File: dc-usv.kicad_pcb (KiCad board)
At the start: 4 copper layers, 160 x 100 mm, 297 parts, among them J1 Output 2.0mm, J2 Output 2.0mm, J3 Output 2.0mm, J5 HanRun_HR911105A, J6 USB_C_Receptacle_USB2.0, J7 Input 2.0mm, J8 Input 2.5mm, J9 USB_C_Receptacle_USB2.0, Q1 AON7544, Q10 AO4407A, Q11 2N7002, Q12 MMBT3904, Q13 2N7002, Q14 2N7002, Q15 2N7002, Q16 2N7002, Q17 2N7002, Q18 MMBT3904, Q19 AO4407A, Q2 AO3401A, Q20 2N7002, Q21 AO4407A, Q22 2N7002, Q23 AO4407A, Q24 2N7002, Q25 AO3401A, Q26 AO3401A, Q27 2N7002, Q28 MMBT3904, Q29 MMBT3904, Q3 AON7544, Q30 MMBT3904, Q31 2N7002, Q32 AO4407A, Q33 MMBT3904, Q34 2N7002, Q35 AO4407A, Q36 MMBT3904, Q37 2N7002, Q38 AO4407A, Q4 AON7544, Q5 AON7544, Q6 CSD17308Q3, Q7 CSD17308Q3, Q8 AO4407A, Q9 2N7002, SW1 SW_DIP_x02, U1 BQ40z50-R2, U10 LAN8720A, U11 74HC595, U12 SY8105, U13 LM75B, U14 INA219AxD, U15 INA219AxD, U16 CH340G, U2 LM75B, U3 BQ24715, U4 TPS61178x, U5 INA219AxD, U6 INA219AxD, U7 LM75B, U8 SY8120B1ABC, U9 ESP32-WROOM-32E, Y1 12MHz

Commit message: Charger and step-down component placement
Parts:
- removed Q26: AO3401A, Package_TO_SOT_SMD:SOT-23
- removed Q27: 2N7002, Package_TO_SOT_SMD:SOT-23
- removed R95: 100kR, Resistor_SMD:R_0402_1005Metric
- added D15: B5819W, Diode_SMD:D_SOD-123, F.Cu at (58.6, 70.1)
- added D16: P6SMB6.8CA, Diode_SMD:D_SMB, F.Cu at (168.1, 109.8)
- C77, C79: value 100nF HV -> 100nF; footprint Capacitor_SMD:C_0603_1608Metric -> Capacitor_SMD:C_0402_1005Metric
- moved R56 231.2 mm to (7.11, 46.9)
- moved R102 230.9 mm to (37.5, 26.9)
- moved Q29 229.7 mm to (38.3, 30.8), turned to -90 degrees
- moved R58 227.6 mm to (7.20, 50.7)
- moved Q28 223.3 mm to (41.8, 30.8), turned to -90 degrees
- moved R60 217.9 mm to (7.25, 53.7)
- moved R101 216.2 mm to (37.5, 28.2)
- moved C16 198.4 mm to (79.7, 84.3), turned to -90 degrees
- moved R17 198.1 mm to (81.8, 101.4)
- moved R61 197.6 mm to (40.8, 79.5), turned to 90 degrees
- moved R22 196.4 mm to (74.0, 99.9), turned to 180 degrees
- moved C12 194.5 mm to (79.4, 95.7)
- moved R53 194.3 mm to (37.8, 33.4)
- moved R93 193.2 mm to (55.8, 69.9), turned to 90 degrees
- moved R92 193.1 mm to (57.1, 66.0), turned to -90 degrees
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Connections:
- C77 pad 1: Net-(C77-Pad1) -> GND
- C77 pad 2: GND -> Net-(C78-Pad1)
- C78 pad 1: Net-(C77-Pad1) -> Net-(C78-Pad1)
- C79 pad 1: GND -> Net-(C78-Pad2)
- C79 pad 2: Net-(C78-Pad2) -> GND
- R80 pad 1: Net-(C77-Pad1) -> Net-(C78-Pad1)
- U14 pad 8: Net-(C77-Pad1) -> Net-(C78-Pad1)
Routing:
- net GND: track 3.25 -> 17.3 mm, vias 3 -> 8
- net +3V3: track 0.00 -> 13.2 mm, vias 0 -> 3
- net Net-(C52-Pad1): track 0.00 -> 9.57 mm
- net Net-(C54-Pad2): track 0.00 -> 5.42 mm
- net Net-(C54-Pad1): track 0.00 -> 4.58 mm
- net Net-(C58-Pad2): track 0.00 -> 3.65 mm
- net Net-(R51-Pad1): track 0.00 -> 1.01 mm

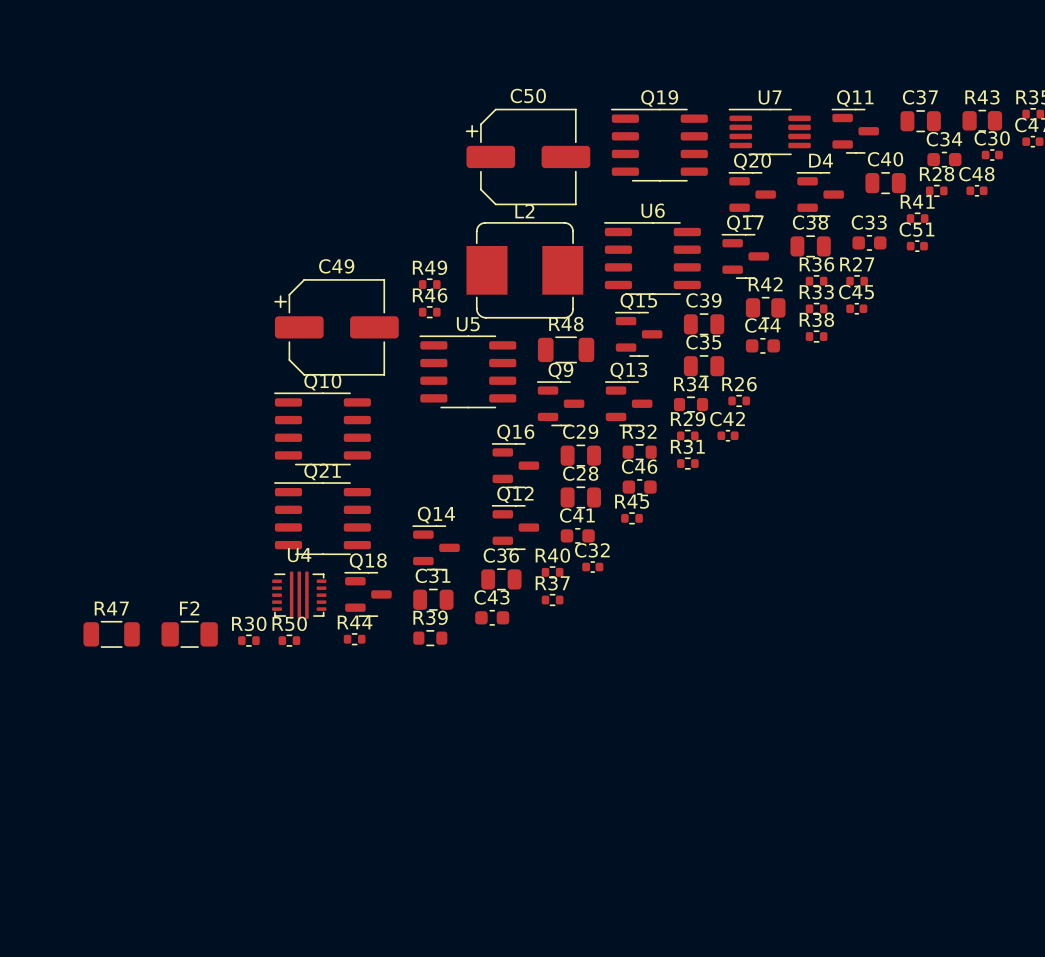
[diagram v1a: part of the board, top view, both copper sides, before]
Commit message: Partial DC out step-up component placement
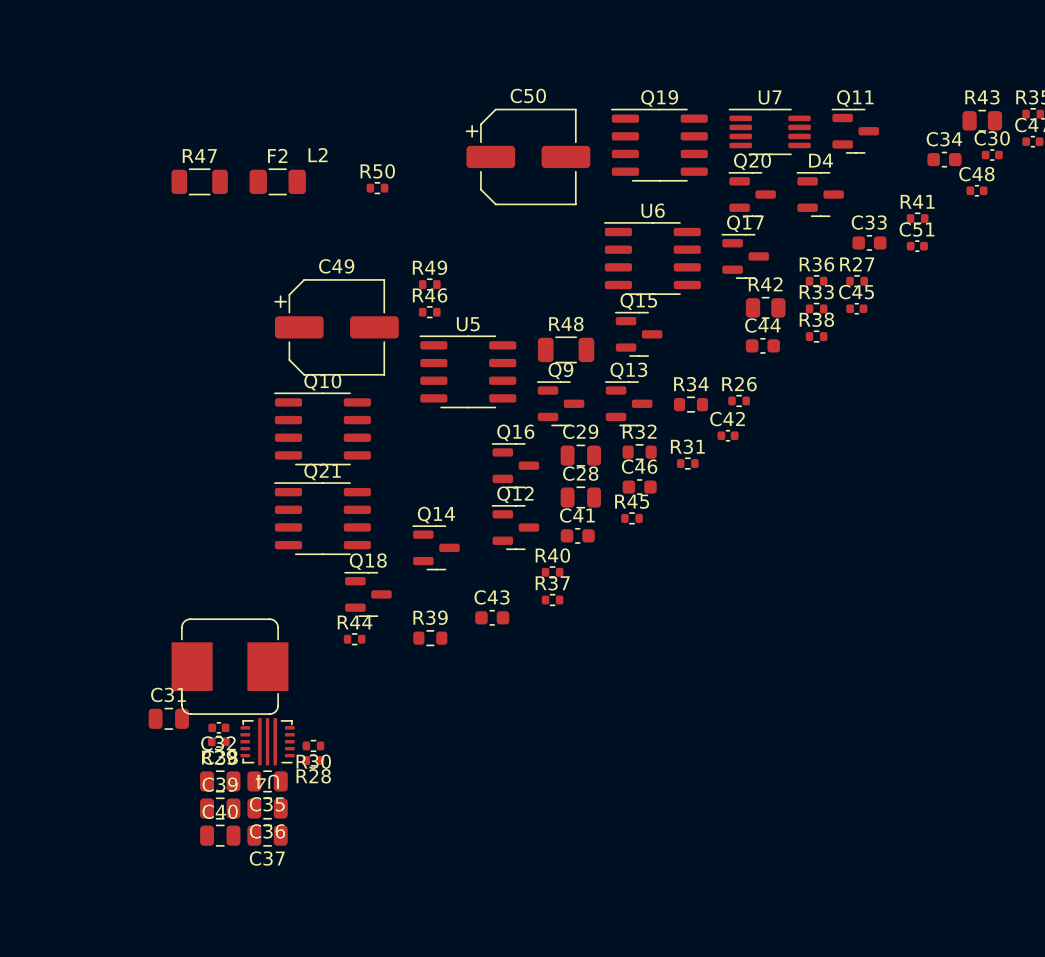
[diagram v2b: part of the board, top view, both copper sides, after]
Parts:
- moved C37 69.6 mm to (205.6, 71.4), turned to 180 degrees
- moved C40 67.0 mm to (202.2, 71.4)
- moved R28 60.7 mm to (208.8, 66.0), turned to 180 degrees
- moved C38 57.3 mm to (202.2, 67.5)
- moved C39 49.2 mm to (202.2, 69.5)
- moved C35 43.3 mm to (205.6, 67.5), turned to 180 degrees
- moved R29 40.2 mm to (202.1, 64.7), turned to 180 degrees
- moved L2 35.5 mm to (202.8, 59.2)
- moved F2 33.1 mm to (206.3, 24.4)
- moved R47 33.1 mm to (200.7, 24.4)
- moved R50 33.1 mm to (213.4, 24.9)
- moved C32 29.3 mm to (202.1, 63.6), turned to 180 degrees
- moved C36 23.5 mm to (205.6, 69.5), turned to 180 degrees
- moved C31 20.9 mm to (198.4, 63.0)
- moved U4 10.8 mm to (205.6, 64.7), turned to 180 degrees
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
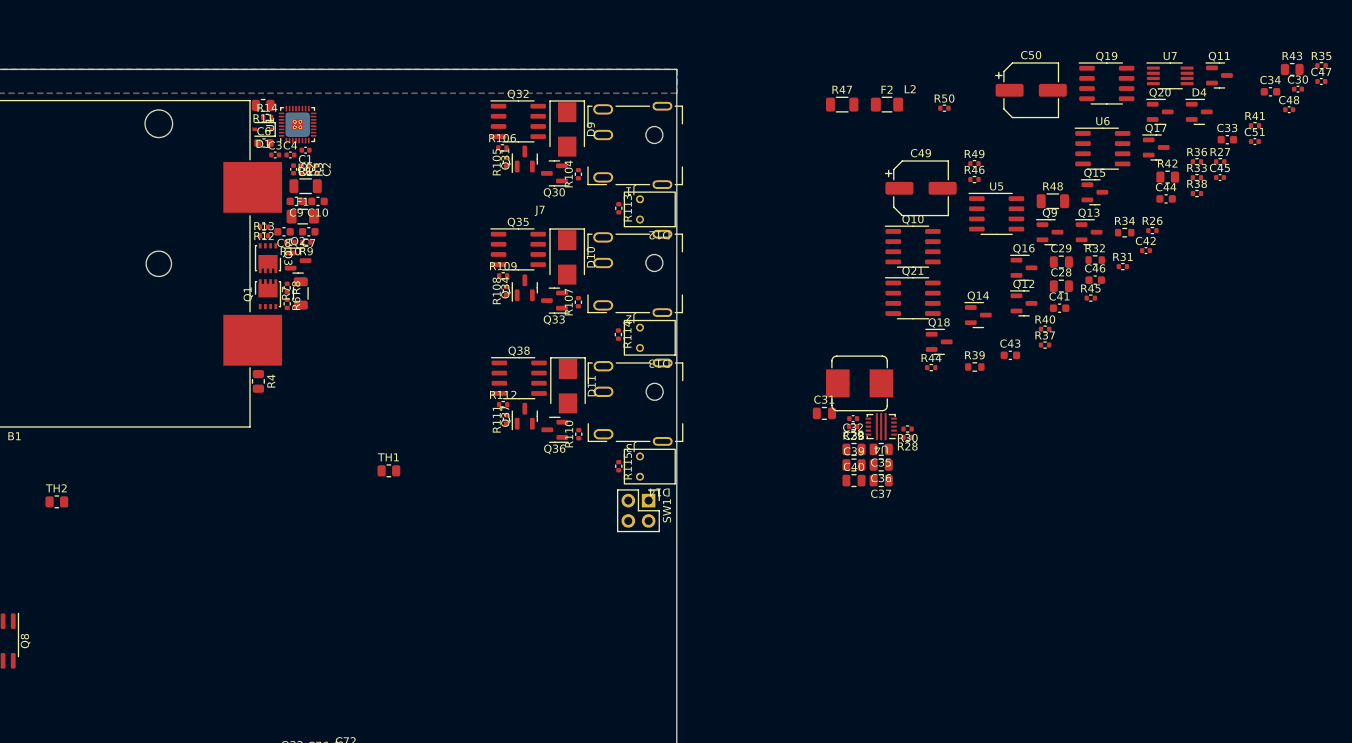
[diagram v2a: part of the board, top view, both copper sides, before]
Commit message: Finish step-up component placement and partial layout
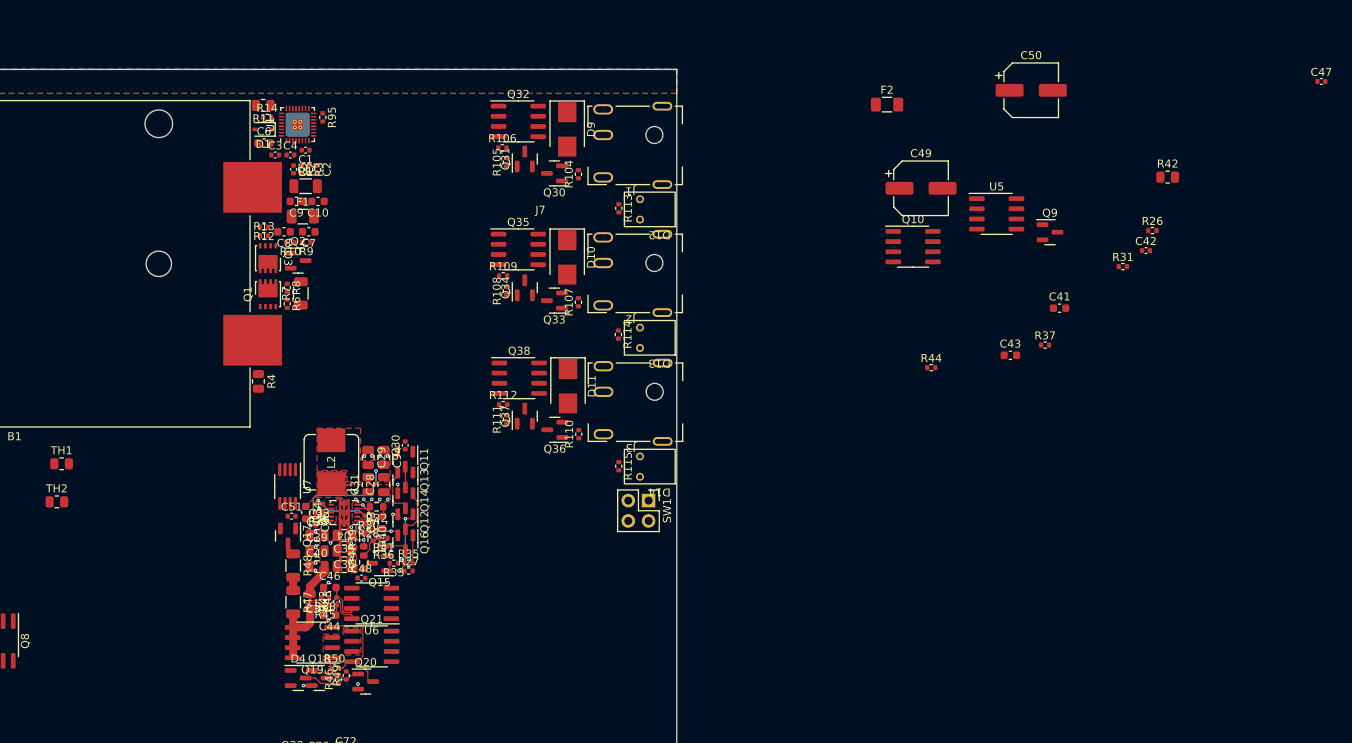
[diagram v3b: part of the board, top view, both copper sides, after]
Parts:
- added C94: 22uF, Capacitor_SMD:C_0805_2012Metric, F.Cu at (143.4, 68.5)
- added C95: 22nF, Capacitor_SMD:C_0402_1005Metric, F.Cu at (134.9, 76.5)
- added R95: 10k, Resistor_SMD:R_0402_1005Metric, F.Cu at (135.8, 26.0)
- moved R43 139.6 mm to (134.2, 86.5), turned to -90 degrees
- moved D4 133.0 mm to (132.7, 96.1)
- moved C34 131.6 mm to (133.6, 75.4), turned to -90 degrees
- moved R35 130.0 mm to (146.5, 81.7)
- moved C48 129.9 mm to (140.6, 83.6)
- moved C51 129.2 mm to (131.8, 75.8)
- moved C45 122.5 mm to (137.5, 86.5), turned to 90 degrees
- moved Q20 122.2 mm to (141.1, 96.5)
- moved U7 121.7 mm to (131.3, 72.2), turned to -90 degrees
- moved Q19 121.4 mm to (134.4, 91.7), turned to 180 degrees
- moved R41 120.5 mm to (143.3, 78.6), turned to 180 degrees
- moved C30 120.2 mm to (146.1, 67.0), turned to 90 degrees
- moved R38 120.1 mm to (136.1, 86.0), turned to 180 degrees
- moved Q17 118.9 mm to (131.4, 78.3), turned to -90 degrees
- moved C44 116.8 mm to (136.6, 88.2), turned to 180 degrees
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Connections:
- net Net-(C34-Pad1) renamed /DC Control/DCLX
- net Net-(C35-Pad2) renamed /DC Control/VOUT
- U1 pad 16: unconnected-(U1-Pad16) -> Net-(U1-Pad16)
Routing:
- net GND: track 17.3 -> 68.5 mm, vias 8 -> 40
- net /DC Control/VOUT: track 0.00 -> 20.1 mm, vias 0 -> 2
- net /Battery Pack/BAT+: track 0.00 -> 17.1 mm, vias 0 -> 2
- net Net-(Q19-Pad4): track 0.00 -> 14.3 mm
- net Net-(Q19-Pad5): track 0.00 -> 11.8 mm
- net Net-(Q12-Pad1): track 0.00 -> 8.90 mm, vias 0 -> 2
- net Net-(C44-Pad1): track 0.00 -> 8.74 mm
- net Net-(R39-Pad2): track 0.00 -> 7.29 mm, vias 0 -> 2
- net Net-(C45-Pad2): track 0.00 -> 6.51 mm
- net Net-(Q13-Pad2): track 0.00 -> 5.42 mm
- net Net-(Q12-Pad3): track 0.00 -> 5.41 mm
- net Net-(D4-Pad3): track 0.00 -> 4.36 mm
- net /DC Control/EN: track 0.00 -> 4.23 mm, vias 0 -> 1
- net Net-(C34-Pad2): track 0.00 -> 3.74 mm
- net Net-(Q18-Pad3): track 0.00 -> 3.72 mm
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- added copper zone on F.Cu, net /Battery Pack/BAT+
- added copper zone on F.Cu, net /DC Control/DCLX
- added copper zone on F.Cu, net /DC Control/VOUT
- added copper zone on F.Cu, net Net-(Q19-Pad1)

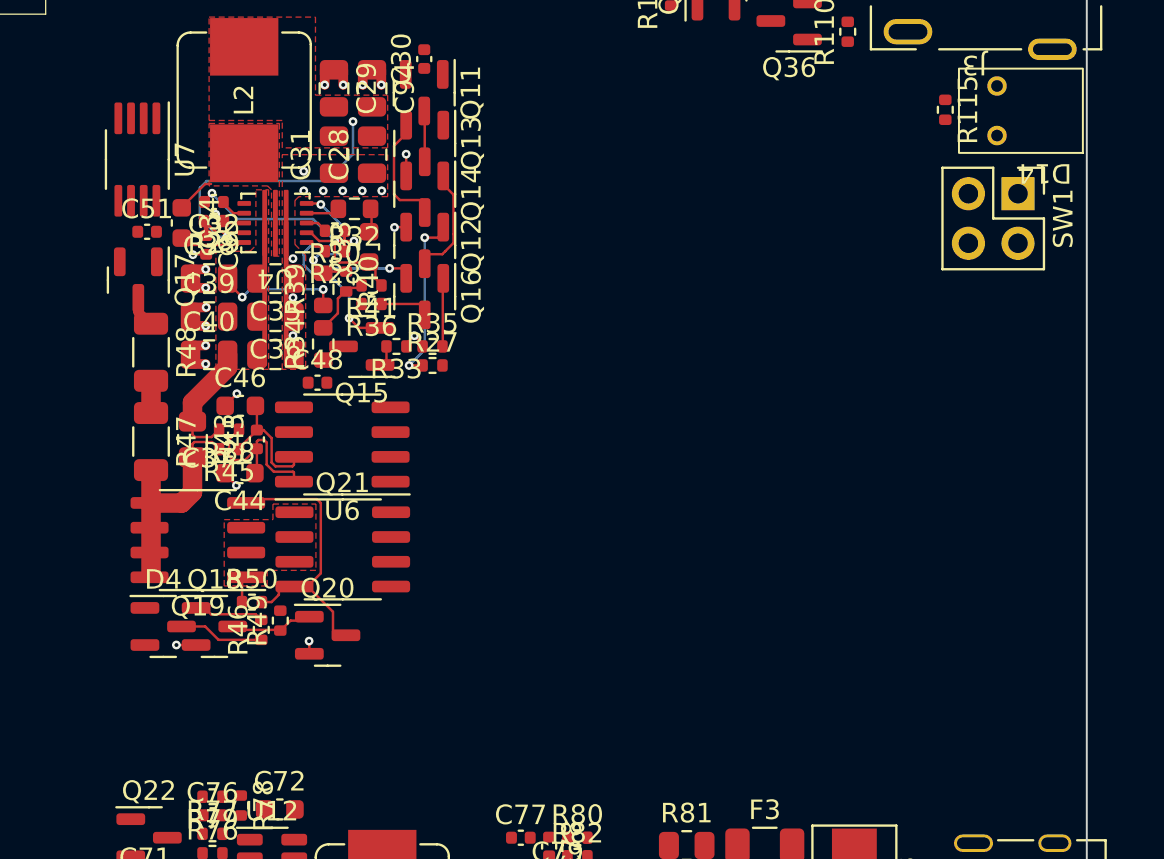
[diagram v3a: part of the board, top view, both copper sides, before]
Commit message: Add 64x48 SSD1306 OLED
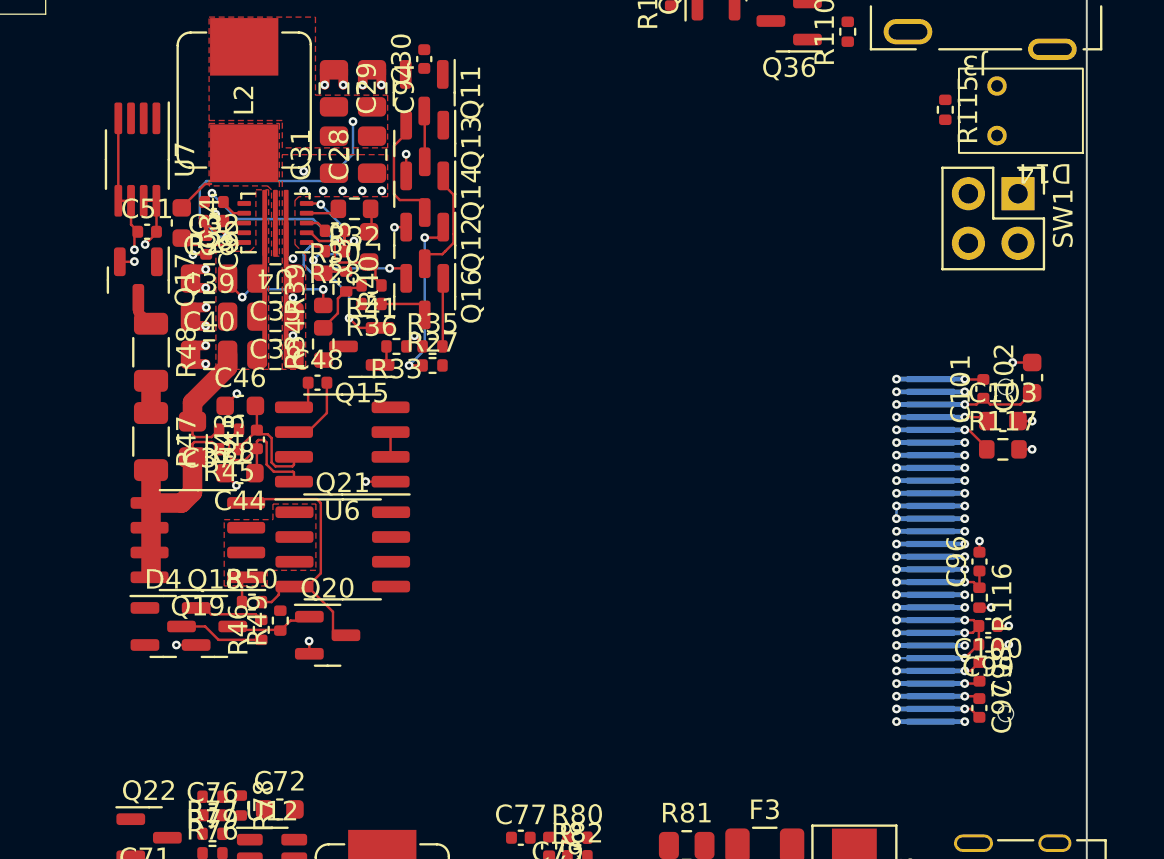
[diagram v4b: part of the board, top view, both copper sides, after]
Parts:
- added C100: 10uF LV, Capacitor_SMD:C_0402_1005Metric, F.Cu at (174.9, 96.0)
- added C101: 100nF, Capacitor_SMD:C_0402_1005Metric, F.Cu at (174.7, 83.9)
- added C102: 4.7uF HV, Capacitor_SMD:C_0603_1608Metric, F.Cu at (177.2, 83.3)
- added C103: 2.2uF, Capacitor_SMD:C_0603_1608Metric, F.Cu at (175.7, 85.5)
- added C96: 100nF, Capacitor_SMD:C_0402_1005Metric, F.Cu at (174.5, 92.8)
- added C97: 1uF, Capacitor_SMD:C_0402_1005Metric, F.Cu at (174.5, 100.2)
- added C98: 1uF, Capacitor_SMD:C_0402_1005Metric, F.Cu at (174.5, 98.4)
- added C99: 100nF, Capacitor_SMD:C_0402_1005Metric, F.Cu at (174.9, 97.0)
- added R116: 100kR, Resistor_SMD:R_0402_1005Metric, F.Cu at (174.5, 94.6)
- added R117: 390kR, Resistor_SMD:R_0603_1608Metric, F.Cu at (175.7, 87.0)
- added U17: N066-6448TSWEG03-H28, Display_OLED:N066-6448TSWEG03-H28, B.Cu at (173.8, 92.2)
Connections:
- U9 pad 24: unconnected-(U9-Pad24) -> /Control Logic/~{OLED_RST}
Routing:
- net GND: track 68.5 -> 135.9 mm, vias 40 -> 77
- net +3V3: track 13.2 -> 32.4 mm, vias 3 -> 11
- net SDA: track 0.00 -> 7.65 mm, vias 0 -> 4
- net Net-(C101-Pad1): track 0.00 -> 7.46 mm, vias 0 -> 2
- net /Control Logic/~{OLED_RST}: track 0.00 -> 5.22 mm, vias 0 -> 2
- net Net-(R117-Pad1): track 0.00 -> 5.08 mm, vias 0 -> 2
- net Net-(C103-Pad1): track 0.00 -> 4.67 mm, vias 0 -> 2
- net Net-(C97-Pad2): track 0.00 -> 4.44 mm, vias 0 -> 2
- net Net-(C98-Pad1): track 0.00 -> 4.44 mm, vias 0 -> 2
- net Net-(C98-Pad2): track 0.00 -> 4.30 mm, vias 0 -> 2
- net Net-(C97-Pad1): track 0.00 -> 4.30 mm, vias 0 -> 2
- net SCL: track 0.00 -> 3.50 mm, vias 0 -> 2
- net SMBD: track 0.00 -> 1.26 mm
